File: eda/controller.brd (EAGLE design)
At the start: 76.2 x 76.2 mm, 97 parts, among them U1 STM32F405/7R, U10 3.3V, U2 ISL83491SOIC, U3 ISL83491SOIC, U4 ISL83491SOIC, U5 ISL83491SOIC, U6 LM3525, U7 BLE-HM-10, U8 XBEE-1NOSILK, U9 TPS54227DDA, X1 MICROSD-SOCKETAMPHENOL, Y1 8 MHz/C_L=18 pF

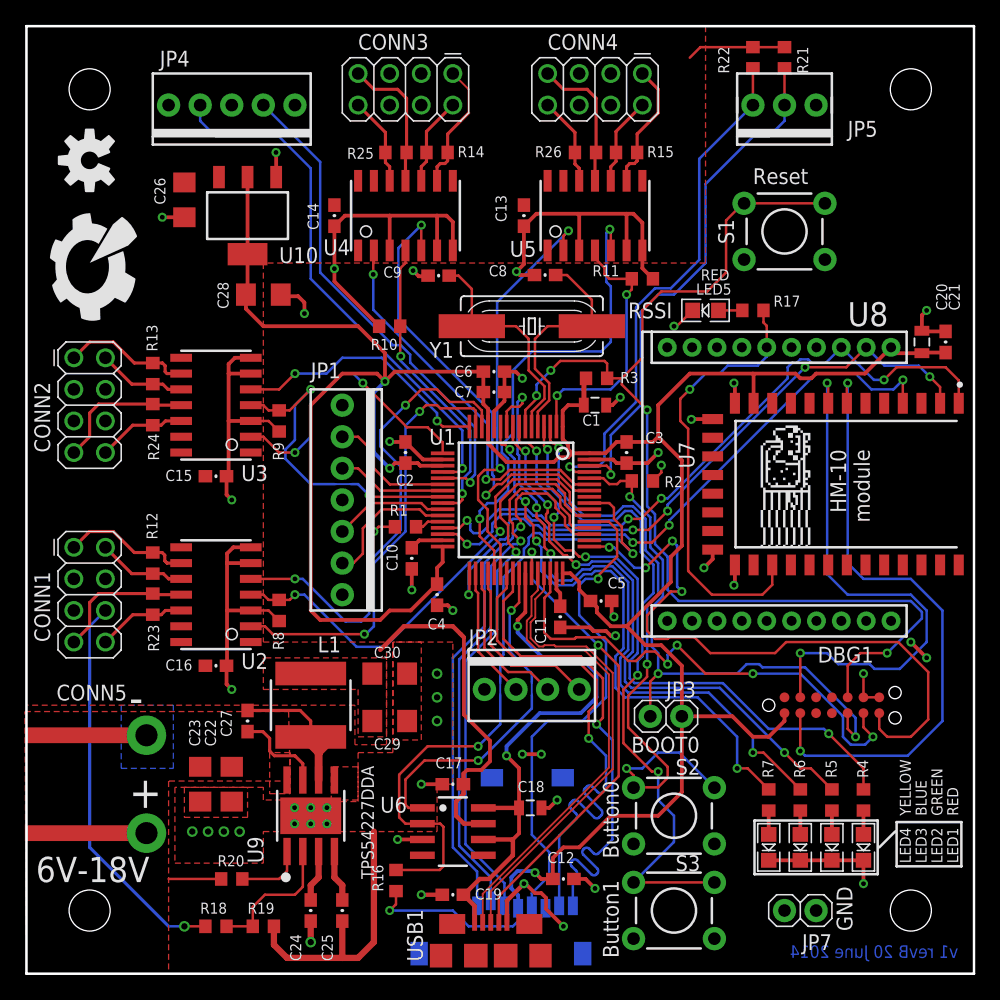
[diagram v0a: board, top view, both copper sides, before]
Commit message: Change smartsensor connectors to 2x5 on controller board
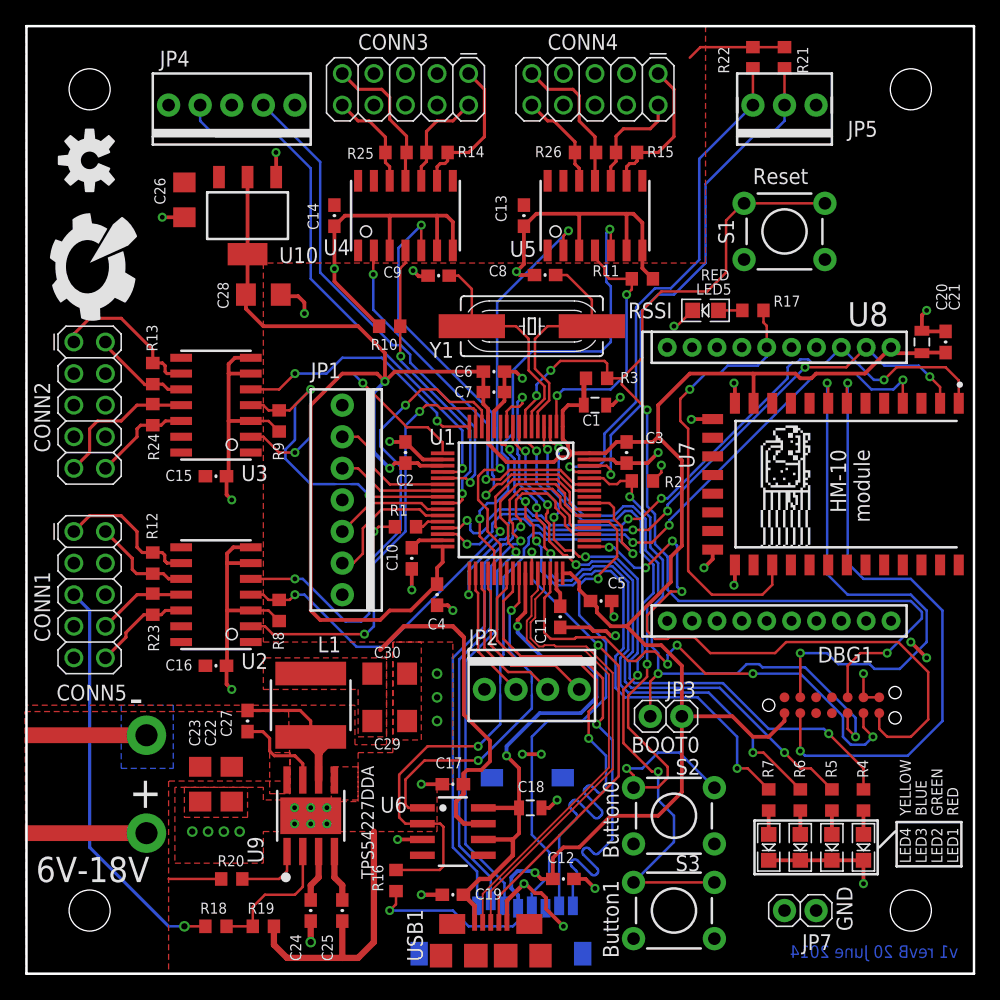
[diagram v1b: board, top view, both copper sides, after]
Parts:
- CONN1, CONN2, CONN3, CONN4: value SENSOR_CONPTH -> (none); device pie:2X4 -> pie:2X5
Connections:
- net 5V: now also CONN1.5, CONN2.5, CONN3.5, CONN4.5; no longer CONN1.3, CONN2.3, CONN3.3, CONN4.3
- net B_RX1_N: now also CONN1.9; no longer CONN1.7
- net B_RX1_P: now also CONN1.10; no longer CONN1.8
- net B_RX2_N: now also CONN2.9; no longer CONN2.7
- net B_RX2_P: now also CONN2.10; no longer CONN2.8
- net B_RX3_N: now also CONN3.9; no longer CONN3.7
- net B_RX3_P: now also CONN3.10; no longer CONN3.8
- net B_RX4_N: now also CONN4.9; no longer CONN4.7
- net B_RX4_P: now also CONN4.10; no longer CONN4.8
- net GND: now also CONN1.3, CONN1.7, CONN1.8, CONN2.3, CONN2.7, CONN2.8, CONN3.3, CONN3.7, CONN3.8, CONN4.3, CONN4.7, CONN4.8; no longer CONN1.5, CONN2.5, CONN3.5, CONN4.5
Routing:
- net B_RX1_N: track 11.4 -> 7.22 mm
- net A_TX3_P: track 10.4 -> 12.6 mm
- net A_TX2_P: track 10.5 -> 12.5 mm
- net A_TX4_N: track 7.14 -> 8.93 mm
- net A_TX4_P: track 10.4 -> 11.9 mm
- net A_TX3_N: track 7.14 -> 8.41 mm
- net 5V: track 67.2 -> 68.4 mm
- net A_TX1_P: track 10.5 -> 11.7 mm
- net B_RX3_P: track 7.14 -> 8.19 mm
- net A_TX1_N: track 7.14 -> 8.19 mm
- net B_RX2_P: track 7.14 -> 8.04 mm
- net B_RX4_P: track 7.14 -> 7.97 mm
- net B_RX1_P: track 7.14 -> 7.89 mm
- net A_TX2_N: track 7.14 -> 7.85 mm
- net B_RX4_N: track 11.4 -> 12.0 mm
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
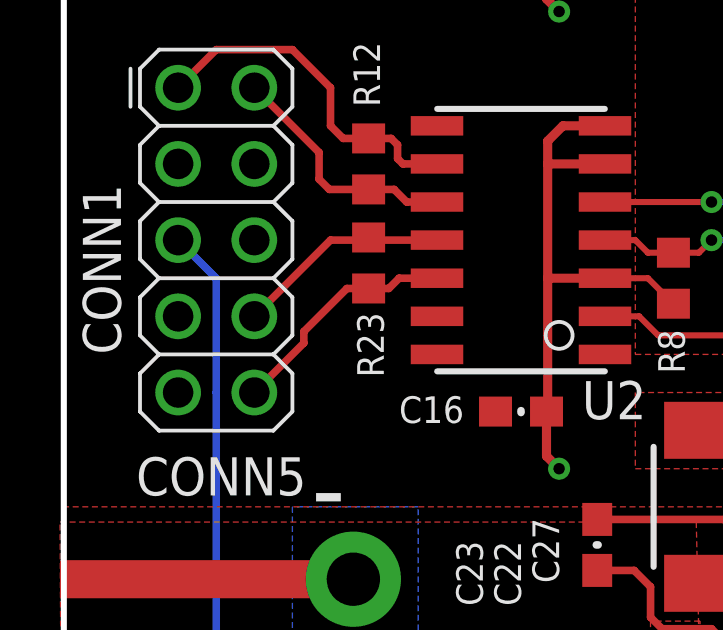
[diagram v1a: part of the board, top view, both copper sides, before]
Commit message: Minor routing fixes on grizzly and controller.
Edit rqou: Hopefully fixed fun merge problems between this commit
and Andrew Wang's.
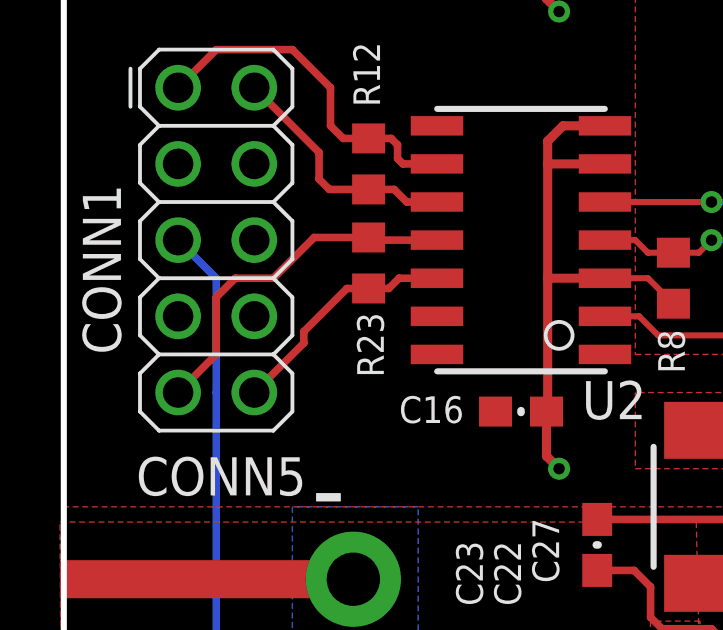
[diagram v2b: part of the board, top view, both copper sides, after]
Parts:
- CONN1, CONN2, CONN3, CONN4: value (none) -> SENSOR_CON_5PINPTH
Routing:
- net B_RX1_N: track 7.22 -> 11.9 mm
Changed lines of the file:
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@@
 <attribute name="PIE-INT-REF-NUM" value="CAPACITOR-GENERIC" x="15.24" y="24.765" size="1.778" layer="27" display="off"/>
 </element>
-<element name="CONN1" library="pie" package="2X5" value="" x="5.08" y="30.48" smashed="yes" rot="R270">
+<element name="CONN1" library="pie" package="2X5" value="SENSOR_CON_5PINPTH" x="5.08" y="30.48" smashed="yes" rot="R270">
 <attribute name="NAME" x="1.905" y="26.67" size="1.27" layer="25" font="vector" ratio="10" rot="R90"/>
 </element>
-<element name="CONN2" library="pie" package="2X5" value="" x="5.08" y="45.72" smashed="yes" rot="R270">
+<element name="CONN2" library="pie" package="2X5" value="SENSOR_CON_5PINPTH" x="5.08" y="45.72" smashed="yes" rot="R270">
 <attribute name="NAME" x="1.905" y="41.91" size="1.27" layer="25" font="vector" ratio="10" rot="R90"/>
 </element>
-<element name="CONN3" library="pie" package="2X5" value="" x="30.48" y="71.12" smashed="yes" rot="R180">
+<element name="CONN3" library="pie" package="2X5" value="SENSOR_CON_5PINPTH" x="30.48" y="71.12" smashed="yes" rot="R180">
 <attribute name="NAME" x="26.67" y="74.295" size="1.27" layer="25" font="vector" ratio="10"/>
 </element>
-<element name="CONN4" library="pie" package="2X5" value="" x="45.72" y="71.12" smashed="yes" rot="R180">
+<element name="CONN4" library="pie" package="2X5" value="SENSOR_CON_5PINPTH" x="45.72" y="71.12" smashed="yes" rot="R180">
 <attribute name="NAME" x="41.91" y="74.295" size="1.27" layer="25" font="vector" ratio="10"/>
 </element>
@@
 <wire x1="10.248" y1="30.48" x2="10.16" y2="30.568" width="0.254" layer="1"/>
 <contactref element="CONN1" pad="9"/>
-<wire x1="10.16" y1="30.568" x2="10.072" y2="30.48" width="0.254" layer="1"/>
-<wire x1="10.072" y1="30.48" x2="8.89" y2="30.48" width="0.254" layer="1"/>
-<wire x1="8.89" y1="30.48" x2="6.35" y2="27.94" width="0.254" layer="1"/>
-<wire x1="3.81" y1="25.4" x2="6.35" y2="27.94" width="0" layer="19" extent="1-1"/>
+<wire x1="10.16" y1="30.568" x2="8.343" y2="30.568" width="0.254" layer="1"/>
+<wire x1="8.343" y1="30.568" x2="6.985" y2="29.21" width="0.254" layer="1"/>
+<wire x1="6.985" y1="29.21" x2="5.715" y2="29.21" width="0.254" layer="1"/>
+<wire x1="5.715" y1="29.21" x2="5.08" y2="28.575" width="0.254" layer="1"/>
+<wire x1="5.08" y1="28.575" x2="5.08" y2="26.67" width="0.254" layer="1"/>
+<wire x1="5.08" y1="26.67" x2="3.81" y2="25.4" width="0.254" layer="1"/>
 </signal>
 <signal name="B_RX1_P">
